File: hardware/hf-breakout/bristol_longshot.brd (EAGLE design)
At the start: 31 x 50 mm, 22 parts, among them U1 SAM_D20E

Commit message: HF board done
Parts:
- removed C15, C16: 100nF, microbuilder_v3:_0402
- removed R8, R9: 10kΩ, microbuilder_v3:_0402
- removed U$1: SI5356, si5356:QFN24_4MM
- removed U$23: TG-5006CJ, fbri:TC-5006CJ
- removed X1: (no value), microbuilder_v3:SMA90_DIP
- added C10: 100pF, microbuilder_v3:_0402
- added C11: 1µF, microbuilder_v3:_0402
- added C4, C5, C6, C7, C8, C9: 100nF, microbuilder_v3:_0402
- added DD, SS: 0Ω, microbuilder_v3:_0402
- added FB1: (no value), microbuilder_v3:_0402
- added IC3: TLV70018DCK, tlv700:SC70-5L
- added J$1, J$2: SMA_EDGE, SparkFun:SMA-EDGE
- added JP1: (no value), SparkFun:1X03_LOCK
- added L5: 100nH, microbuilder_v3:_0402
- added U2: SI5356, si5356:QFN24_4MM
- added U3: AD8354, fbri:LFCSP_VD_8
- added U6: TG-5006CJ, fbri:TC-5006CJ
- C12: value 100nF -> 1µF
- R4: value 0Ω -> 10kΩ
- R5: value 0Ω -> 15kΩ
- R6: value 15kΩ -> 220Ω
- R7: value 15kΩ -> DNP
- moved JTAG1 20.7 mm to (3.50, 33.0), turned to 0 degrees
- moved C12 17.3 mm to (14.5, 33.5), turned to 0 degrees
- moved R3 15.4 mm to (7.75, 18.8), turned to 90 degrees
- moved R4 14.4 mm to (6.50, 15.5), turned to 180 degrees
- moved FB2 13.3 mm to (13.8, 18.5), turned to 270 degrees
- moved U1 13.2 mm to (11.5, 27.0), turned to 90 degrees
- moved R2 12.7 mm to (13.5, 13.5), turned to 0 degrees
- moved R6 12.7 mm to (14.0, 31.2), turned to 90 degrees
- moved R7 12.5 mm to (5.75, 22.8)
- moved R5 11.3 mm to (8.75, 18.8), turned to 270 degrees
- moved C3 11.2 mm to (11.8, 19.5)
- moved C1 10.8 mm to (13.5, 16.2), turned to 0 degrees
- moved C2 10.6 mm to (5.50, 16.5)
- moved R1 8.00 mm to (6.50, 13.5), turned to 180 degrees
- moved D1 5.00 mm to (15.0, 31.0), turned to 0 degrees
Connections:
- removed net !OE: R7.2, R8.1, U$1.6
- removed net !OE_CTRL: R8.2
- new net 3.3V: C11.1, IC3.1, IC3.3, JP1.1, JTAG1.1
- new net AMPL_OUT: C5.1, L5.1, U3.7
- new net AMPL_VPOS: C10.1, C6.1, FB1.1, L5.2, U3.6
- new net HF: C5.2, J$2.SIG
- new net HF_CLK: C4.1, U2.17
- new net INPT: C4.2, U3.3
- new net LED_R: R6.1, U1.16
- new net N$1: C12.1, IC3.5, JP1.3
- net 1.8V: now also C8.1, FB1.2, JP1.2, R4.2, U2.11, U2.15, U2.16, U2.20, U2.24, U2.7; no longer C15.1, JTAG1.1, R9.2, U$1.11, U$1.15, U$1.16, U$1.20, U$1.24, U$1.7
- net CLKIN: now also DD.1, U2.4; no longer R5.1, U$1.4
- net CLKIN_SMA: now also DD.2, J$1.SIG, R7.2; no longer R5.2, X1.ANTENNA
- net GND: now also C10.2, C11.2, C6.2, C7.2, C8.2, C9.2, IC3.2, J$1.GND@0, J$1.GND@1, J$1.GND@2, J$1.GND@3, J$2.GND@0, J$2.GND@1, J$2.GND@2, J$2.GND@3, R5.1, SS.2, U2.23, U2.3, U2.6, U2.PAD, U3.1, U3.4, U3.5, U3.8, U3.EPAD, U6.2; no longer C15.2, C16.2, R4.2, R6.1, U$1.23, U$1.3, U$1.PAD, U$23.2, X1.GND1, X1.GND2, X1.GND3, X1.GND4
- net INTR: now also R4.1, U2.8; no longer R9.1, U$1.8
- net LED: now also R6.2; no longer U1.16
- net SCL: now also U1.6, U2.12; no longer U$1.12
- net SDA: now also U1.5, U2.19; no longer U$1.19
- net SSC_DIS: now also R5.2, U2.5; no longer R6.2, U$1.5
- net TCXO_OUT: now also U6.3; no longer U$23.3
- net TCXO_VDD: now also C7.1, U6.4; no longer C12.1, U$23.4
- net VDD_CORE: now also C9.1; no longer C16.1
- net XA: now also U2.1; no longer U$1.1
- net XB: now also SS.1, U2.2; no longer R4.1, U$1.2
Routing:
- net 1.8V: track 0.00 -> 75.8 mm, vias 0 -> 4
- net SCL: track 0.00 -> 23.9 mm, vias 0 -> 2
- net 3.3V: track 0.00 -> 18.0 mm, vias 0 -> 2
- net SDA: track 0.00 -> 17.3 mm
- net SWDIO: track 0.00 -> 16.3 mm
- net SWDCLK: track 0.00 -> 15.0 mm
- net CLKIN_SMA: track 0.00 -> 9.52 mm
- net GND: track 1.25 -> 10.4 mm, vias 5 -> 60
- net !RESET: track 0.00 -> 8.12 mm
- net AMPL_VPOS: track 0.00 -> 4.37 mm
- net N$1: track 0.00 -> 3.95 mm
- net HF: track 0.00 -> 2.76 mm
- net SSC_DIS: track 0.00 -> 2.45 mm
- net TCXO_VDD: track 0.00 -> 2.26 mm
- net AMPL_OUT: track 0.00 -> 2.08 mm
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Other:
- board size 31 x 50 mm -> 16 x 40 mm
- board text added: "1.8V"
- board text added: "3.3V"
- board text added: "ARM-SWD"
- board text added: "CLKIN"
- board text added: "HF OUT"

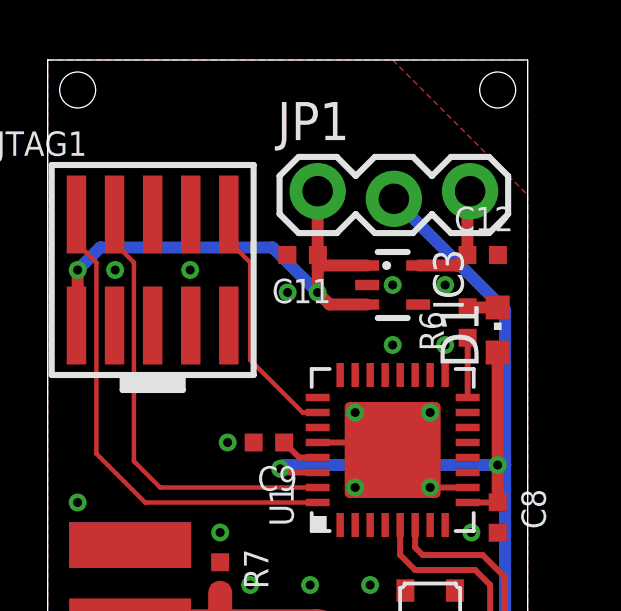
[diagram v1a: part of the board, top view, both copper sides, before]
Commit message: Updated many parts lists, updated bard numbering, removed makefiles for inactive things
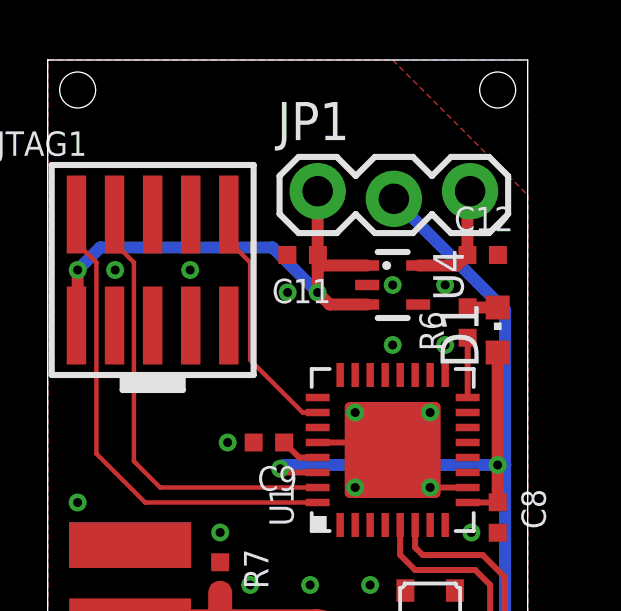
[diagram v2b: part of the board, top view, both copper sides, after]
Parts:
- renumbered IC3 to U4
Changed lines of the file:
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@@
 <?xml version="1.0" encoding="utf-8"?>
 <!DOCTYPE eagle SYSTEM "eagle.dtd">
-<eagle version="6.5.0">
+<eagle version="7.3.0">
 <drawing>
 <settings>
@@
 <pass name="Default">
 <param name="RoutingGrid" value="50mil"/>
+<param name="AutoGrid" value="1"/>
+<param name="Efforts" value="0"/>
+<param name="TopRouterVariant" value="1"/>
 <param name="tpViaShape" value="round"/>
 <param name="PrefDir.1" value="|"/>
@@
 <element name="L5" library="microbuilder_v3" package="_0402" value="100nH" x="11" y="7.25" rot="R180"/>
 <element name="J$2" library="SparkFun" package="SMA-EDGE" value="SMA_EDGE" x="9" y="2.5"/>
-<element name="IC3" library="tlv700" package="SC70-5L" value="TLV70018DCK" x="11.5" y="32.5" rot="R270"/>
+<element name="U4" library="tlv700" package="SC70-5L" value="TLV70018DCK" x="11.5" y="32.5" rot="R270"/>
 <element name="JP1" library="SparkFun" package="1X03_LOCK" value="" x="9" y="35.5"/>
 <element name="C11" library="microbuilder_v3" package="_0402" value="1µF" x="8.5" y="33.5" rot="R180"/>
@@
 <via x="5" y="15" extent="1-16" drill="0.3"/>
 <via x="5" y="13" extent="1-16" drill="0.3"/>
-<contactref element="IC3" pad="2"/>
+<contactref element="U4" pad="2"/>
 <contactref element="C11" pad="2"/>
 <contactref element="C12" pad="2"/>
@@
 <signal name="3.3V">
 <contactref element="JTAG1" pad="1"/>
-<contactref element="IC3" pad="1"/>
-<contactref element="IC3" pad="3"/>
+<contactref element="U4" pad="1"/>
+<contactref element="U4" pad="3"/>
 <contactref element="JP1" pad="1"/>
 <contactref element="C11" pad="1"/>
@@
 </signal>
 <signal name="N$1">
-<contactref element="IC3" pad="5"/>
+<contactref element="U4" pad="5"/>
 <contactref element="JP1" pad="3"/>
 <contactref element="C12" pad="1"/>
